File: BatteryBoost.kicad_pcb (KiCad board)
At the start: 2 copper layers, 78 x 40 mm, 27 parts, among them J1 USB_B_Micro, J2 Conn_01x02, J3 Conn_01x02, SW1 SW_SPDT, U1 SP34063AEN, U2 TP4056

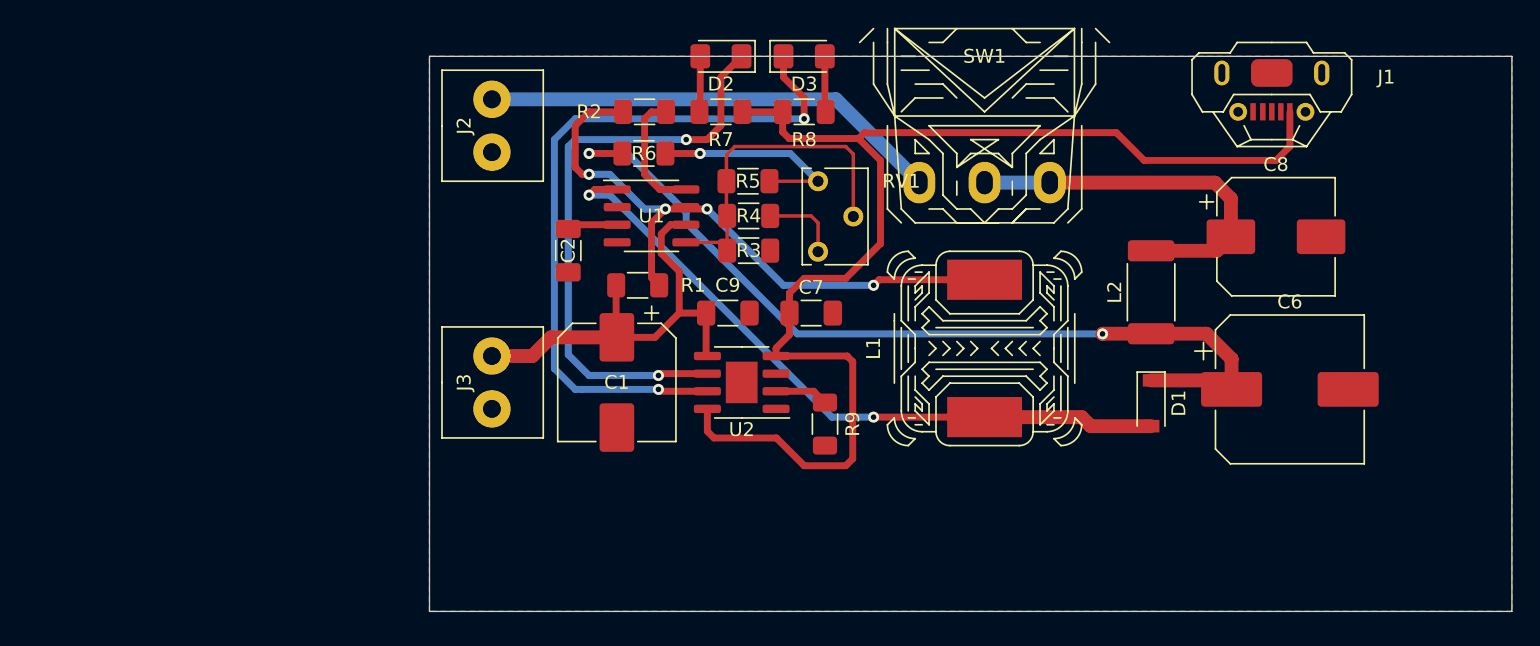
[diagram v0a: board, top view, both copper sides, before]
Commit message: update schematic and layout
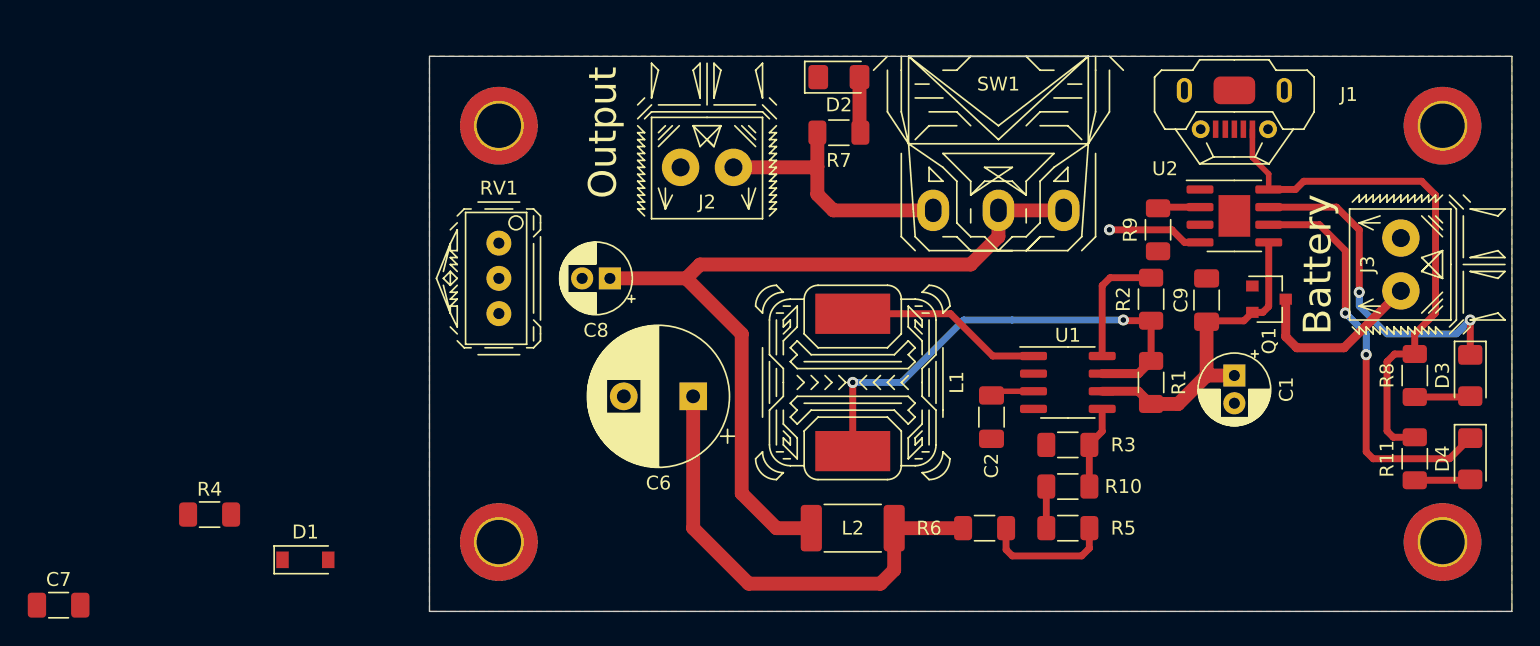
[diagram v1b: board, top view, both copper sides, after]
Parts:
- added D4: Blue LED, Diode_SMD:D_1206_3216Metric_Pad1.42x1.75mm_HandSolder, F.Cu at (75.0, 29.0)
- added J4: Mounting Hole, MountingHole:MountingHole_3.2mm_M3_DIN965_Pad_TopBottom, F.Cu at (5.00, 5.00)
- added J5: Mounting Hole, MountingHole:MountingHole_3.2mm_M3_DIN965_Pad_TopBottom, F.Cu at (73.0, 35.0)
- added J6: Mounting Hole, MountingHole:MountingHole_3.2mm_M3_DIN965_Pad_TopBottom, F.Cu at (73.0, 5.00)
- added J7: Mounting Hole, MountingHole:MountingHole_3.2mm_M3_DIN965_Pad_TopBottom, F.Cu at (5.00, 35.0)
- added Q1: Q_PMOS_GSD, Package_TO_SOT_SMD:SC-59, F.Cu at (60.5, 17.5)
- added R10: 499k 0.25W 1%, Resistor_SMD:R_1206_3216Metric_Pad1.30x1.75mm_HandSolder, F.Cu at (46.0, 31.0)
- added R11: 10k, Resistor_SMD:R_1206_3216Metric_Pad1.30x1.75mm_HandSolder, F.Cu at (71.0, 29.0)
- C1, C8: footprint Capacitor_SMD:CP_Elec_8x10 -> Capacitor_THT:CP_Radial_D5.0mm_P2.00mm
- C6: footprint Capacitor_SMD:CP_Elec_10x12.5 -> Capacitor_THT:CP_Radial_D10.0mm_P5.00mm
- D2: value LED -> Blue LED
- D3: value LED -> Red LED
- J1: footprint Fume_Extractor:U-F-M5DD-Y-L -> BatteryBoost:U-F-M5DD-Y-L
- J2, J3: footprint Fume_Extractor:WJ124-3.81-2P -> BatteryBoost:WJ124-3.81-2P
- L1: footprint Fume_Extractor:Inductor_SLH_12x12x8 -> BatteryBoost:Inductor_SLH_12x12x8
- R5: value 508.064k -> 9.1k 1% 0.25W
- RV1: footprint Potentiometer_THT:Potentiometer_Bourns_3266W_Vertical -> BatteryBoost:Potentiometer_3296W-1-504
- SW1: footprint Fume_Extractor:Switch_SS-12D06L5 -> BatteryBoost:Switch_SS-12D06L5
- U2: footprint Package_SO:SOIC-8-1EP_3.9x4.9mm_P1.27mm_EP2.29x3mm -> BatteryBoost:SOIC-8-1EP_3.9x4.9mm_P1.27mm_EP2.29x3mm
- moved J3 66.0 mm to (70.0, 15.0), turned to 90 degrees
- moved D1 62.0 mm to (-8.95, 36.3), turned to 0 degrees
- moved C7 58.2 mm to (-26.7, 39.5)
- moved D3 53.2 mm to (75.0, 23.0), turned to 270 degrees
- moved C8 48.1 mm to (13.0, 16.0), turned to 180 degrees
- moved R8 47.9 mm to (71.0, 23.0), turned to 90 degrees
- moved C1 44.5 mm to (58.0, 23.0)
- moved R4 44.4 mm to (-15.8, 33.0), turned to 0 degrees
- moved C6 43.0 mm to (19.0, 24.5), turned to 180 degrees
- moved R2 38.9 mm to (52.0, 17.5), turned to 270 degrees
- moved R1 37.7 mm to (52.0, 23.5), turned to 270 degrees
- moved U2 37.5 mm to (58.0, 11.5), turned to 0 degrees
- moved R6 36.5 mm to (40.0, 34.0)
- moved C9 34.5 mm to (56.0, 17.6), turned to 90 degrees
- moved R5 34.0 mm to (46.0, 34.0), turned to 180 degrees
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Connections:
- D2 pad 1: Net-(D2-Pad1) -> GND
- J3 pad 1: VBATT -> Net-(J3-Pad1)
- R3 pad 2: Net-(R3-Pad2) -> Net-(R10-Pad2)
- R4 pad 2: Net-(R3-Pad2) -> Net-(R10-Pad2)
- R5 pad 1: Net-(R3-Pad2) -> Net-(R5-Pad1)
- R5 pad 2: Net-(R5-Pad2) -> Net-(R10-Pad1)
- R6 pad 1: Net-(R5-Pad2) -> Net-(R5-Pad1)
- R7 pad 1: Net-(D2-Pad2) -> Net-(J2-Pad1)
- R7 pad 2: +5V -> Net-(D2-Pad2)
- RV1 pad 1: Net-(R5-Pad2) -> Net-(R5-Pad1)
- RV1 pad 2: Net-(R3-Pad2) -> Net-(R10-Pad2)
- U1 pad 2: GND -> Net-(U1-Pad2)
- U1 pad 5: Net-(R3-Pad2) -> Net-(R10-Pad2)
- U2 pad 6: Net-(D2-Pad1) -> Net-(D4-Pad1)
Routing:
- net +5V: track 92.2 -> 45.9 mm, vias 0 -> 1
- net Net-(D2-Pad1): track 42.9 -> 0.00 mm, vias 2 -> 0
- net Net-(D1-Pad2): track 49.6 -> 14.3 mm, vias 2 -> 0
- net +24V: track 27.1 -> 59.0 mm
- net Net-(D4-Pad1): track 0.00 -> 29.7 mm, vias 0 -> 2
- net Net-(C6-Pad1): track 63.6 -> 34.1 mm, vias 2 -> 0
- net Net-(D3-Pad1): track 51.9 -> 24.5 mm
- net Net-(R3-Pad2): track 24.3 -> 0.00 mm
- net Net-(R5-Pad2): track 15.3 -> 0.00 mm, vias 1 -> 0
- net Net-(J2-Pad1): track 33.3 -> 19.3 mm
- net Net-(J3-Pad1): track 0.00 -> 13.0 mm
- net Net-(L1-Pad2): track 46.7 -> 35.1 mm, vias 4 -> 2
- net Net-(R5-Pad1): track 0.00 -> 9.41 mm
- net VBATT: track 31.9 -> 24.2 mm
- net Net-(R10-Pad2): track 0.00 -> 5.98 mm
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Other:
- board text added: "Battery"
- board text added: "Output"
